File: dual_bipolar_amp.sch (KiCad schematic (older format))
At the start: 9 parts, among them U4 OPA2156xD

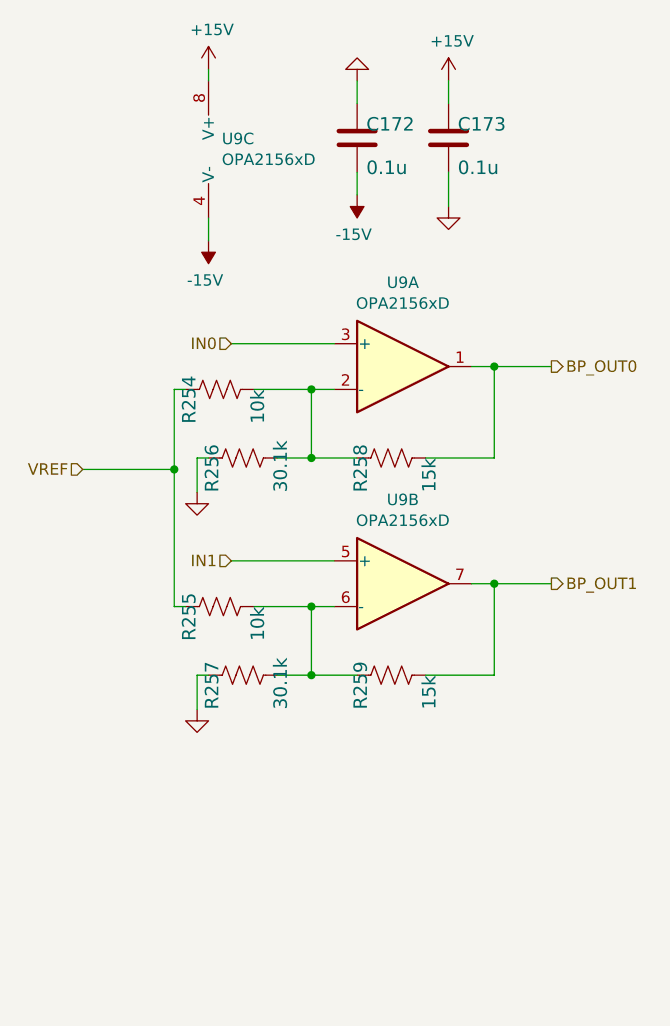
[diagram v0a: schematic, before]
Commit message: finished parts placement; reconnecting pins for less spagheti
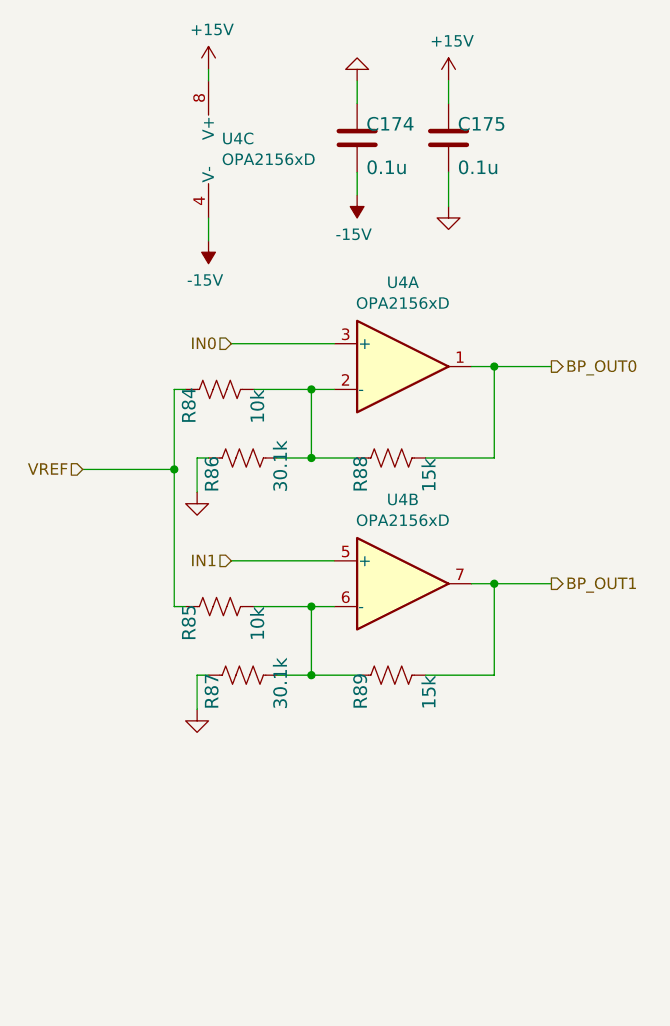
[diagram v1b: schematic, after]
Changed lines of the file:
@@
 $Descr A4 11693 8268
 encoding utf-8
-Sheet 24 26
+Sheet 23 26
 Title ""
 Date ""
@@
 AR Path="/6095BD4C/60EB6FD5/60F31C8B" Ref="U2"  Part="1"
 AR Path="/61B02572/60EB6FD5/60F31C8B" Ref="U9"  Part="1"
-F 0 "U9" H 5600 3617 50  0000 C CNN
+F 0 "U4" H 5600 3617 50  0000 C CNN
 F 1 "OPA2156xD" H 5600 3526 50  0000 C CNN
 F 2 "Package_SO:SOIC-8_3.9x4.9mm_P1.27mm" H 5700 3250 50  0001 C CNN
@@
 AR Path="/6095BD4C/60EB6FD5/60F31C94" Ref="R3"  Part="1"
 AR Path="/61B02572/60EB6FD5/60F31C94" Ref="R254"  Part="1"
-F 0 "R254" H 4650 3450 59  0000 L BNN
+F 0 "R84" H 4650 3450 59  0000 L BNN
 F 1 "10k" H 4650 3150 59  0000 L BNN
 F 2 "Resistor_SMD:R_0603_1608Metric" H 4800 3350 50  0001 C CNN
@@
 AR Path="/6095BD4C/60EB6FD5/60F31C9B" Ref="U2"  Part="3"
 AR Path="/61B02572/60EB6FD5/60F31C9B" Ref="U9"  Part="3"
-F 0 "U9" H 4808 2346 50  0000 L CNN
+F 0 "U4" H 4808 2346 50  0000 L CNN
 F 1 "OPA2156xD" H 4808 2255 50  0000 L CNN
 F 2 "Package_SO:SOIC-8_3.9x4.9mm_P1.27mm" H 4850 2300 50  0001 C CNN
@@
 AR Path="/6095BD4C/60EB6FD5/60F31CA4" Ref="R7"  Part="1"
 AR Path="/61B02572/60EB6FD5/60F31CA4" Ref="R256"  Part="1"
-F 0 "R256" H 4750 3750 59  0000 L BNN
+F 0 "R86" H 4750 3750 59  0000 L BNN
 F 1 "30.1k" H 4750 3450 59  0000 L BNN
 F 2 "Resistor_SMD:R_0603_1608Metric" H 4900 3650 50  0001 C CNN
@@
 AR Path="/6095BD4C/60EB6FD5/60F31CAA" Ref="#GND0250"  Part="1"
 AR Path="/61B02572/60EB6FD5/60F31CAA" Ref="#GND0276"  Part="1"
-F 0 "#GND0276" H 4700 3800 50  0001 C CNN
+F 0 "#GND063" H 4700 3800 50  0001 C CNN
 F 1 "GND" H 4600 3700 59  0001 L BNN
 F 2 "" H 4700 3800 50  0001 C CNN
@@
 AR Path="/6095BD4C/60EB6FD5/60F31CB1" Ref="R13"  Part="1"
 AR Path="/61B02572/60EB6FD5/60F31CB1" Ref="R258"  Part="1"
-F 0 "R258" H 5400 3750 59  0000 L BNN
+F 0 "R88" H 5400 3750 59  0000 L BNN
 F 1 "15k" H 5400 3450 59  0000 L BNN
 F 2 "Resistor_SMD:R_0603_1608Metric" H 5550 3650 50  0001 C CNN
@@
 AR Path="/6095BD4C/60EB6FD5/60F31CB8" Ref="U2"  Part="2"
 AR Path="/61B02572/60EB6FD5/60F31CB8" Ref="U9"  Part="2"
-F 0 "U9" H 5600 4567 50  0000 C CNN
+F 0 "U4" H 5600 4567 50  0000 C CNN
 F 1 "OPA2156xD" H 5600 4476 50  0000 C CNN
 F 2 "Package_SO:SOIC-8_3.9x4.9mm_P1.27mm" H 5700 4200 50  0001 C CNN
@@
 AR Path="/6095BD4C/60EB6FD5/60F31CC1" Ref="R4"  Part="1"
 AR Path="/61B02572/60EB6FD5/60F31CC1" Ref="R255"  Part="1"
-F 0 "R255" H 4650 4400 59  0000 L BNN
+F 0 "R85" H 4650 4400 59  0000 L BNN
 F 1 "10k" H 4650 4100 59  0000 L BNN
 F 2 "Resistor_SMD:R_0603_1608Metric" H 4800 4300 50  0001 C CNN
@@
 AR Path="/6095BD4C/60EB6FD5/60F31CCA" Ref="R8"  Part="1"
 AR Path="/61B02572/60EB6FD5/60F31CCA" Ref="R257"  Part="1"
-F 0 "R257" H 4750 4700 59  0000 L BNN
+F 0 "R87" H 4750 4700 59  0000 L BNN
 F 1 "30.1k" H 4750 4400 59  0000 L BNN
 F 2 "Resistor_SMD:R_0603_1608Metric" H 4900 4600 50  0001 C CNN
@@
 AR Path="/6095BD4C/60EB6FD5/60F31CD0" Ref="#GND0251"  Part="1"
 AR Path="/61B02572/60EB6FD5/60F31CD0" Ref="#GND0277"  Part="1"
-F 0 "#GND0277" H 4700 4750 50  0001 C CNN
+F 0 "#GND098" H 4700 4750 50  0001 C CNN
 F 1 "GND" H 4600 4650 59  0001 L BNN
 F 2 "" H 4700 4750 50  0001 C CNN
@@
 AR Path="/6095BD4C/60EB6FD5/60F31CD7" Ref="R14"  Part="1"
 AR Path="/61B02572/60EB6FD5/60F31CD7" Ref="R259"  Part="1"
-F 0 "R259" H 5400 4700 59  0000 L BNN
+F 0 "R89" H 5400 4700 59  0000 L BNN
 F 1 "15k" H 5400 4400 59  0000 L BNN
 F 2 "Resistor_SMD:R_0603_1608Metric" H 5550 4600 50  0001 C CNN
@@
 AR Path="/6095BD4C/60EB6FD5/60F31CDD" Ref="#PWR0235"  Part="1"
 AR Path="/61B02572/60EB6FD5/60F31CDD" Ref="#PWR0270"  Part="1"
-F 0 "#PWR0270" H 4750 1800 50  0001 C CNN
+F 0 "#PWR0240" H 4750 1800 50  0001 C CNN
 F 1 "+15V" H 4765 2123 50  0000 C CNN
 F 2 "" H 4750 1950 50  0001 C CNN
@@
 AR Path="/6095BD4C/60EB6FD5/60F31CE3" Ref="#PWR0236"  Part="1"
 AR Path="/61B02572/60EB6FD5/60F31CE3" Ref="#PWR0271"  Part="1"
-F 0 "#PWR0271" H 4750 2800 50  0001 C CNN
+F 0 "#PWR0241" H 4750 2800 50  0001 C CNN
 F 1 "-15V" H 4765 2873 50  0000 C CNN
 F 2 "" H 4750 2700 50  0001 C CNN
@@
 AR Path="/6095BD4C/60EB6FD5/60F31CED" Ref="C5"  Part="1"
 AR Path="/61B02572/60EB6FD5/60F31CED" Ref="C172"  Part="1"
-F 0 "C172" H 5440 2275 59  0000 L BNN
+F 0 "C174" H 5440 2275 59  0000 L BNN
 F 1 "0.1u" H 5440 2085 59  0000 L BNN
 F 2 "Capacitor_SMD:C_0603_1608Metric" H 5400 2250 50  0001 C CNN
@@
 AR Path="/6095BD4C/60EB6FD5/60F31CF7" Ref="C6"  Part="1"
 AR Path="/61B02572/60EB6FD5/60F31CF7" Ref="C173"  Part="1"
-F 0 "C173" H 5840 2275 59  0000 L BNN
+F 0 "C175" H 5840 2275 59  0000 L BNN
 F 1 "0.1u" H 5840 2085 59  0000 L BNN
 F 2 "Capacitor_SMD:C_0603_1608Metric" H 5800 2250 50  0001 C CNN
@@
 AR Path="/6095BD4C/60EB6FD5/60F31CFD" Ref="#PWR0238"  Part="1"
 AR Path="/61B02572/60EB6FD5/60F31CFD" Ref="#PWR0272"  Part="1"
-F 0 "#PWR0272" H 5400 2600 50  0001 C CNN
+F 0 "#PWR0244" H 5400 2600 50  0001 C CNN
 F 1 "-15V" H 5415 2673 50  0000 C CNN
 F 2 "" H 5400 2500 50  0001 C CNN
@@
 AR Path="/6095BD4C/60EB6FD5/60F31D03" Ref="#GND0252"  Part="1"
 AR Path="/61B02572/60EB6FD5/60F31D03" Ref="#GND0278"  Part="1"
-F 0 "#GND0278" H 5400 2000 50  0001 C CNN
+F 0 "#GND099" H 5400 2000 50  0001 C CNN
 F 1 "GND" H 5300 1900 59  0001 L BNN
 F 2 "" H 5400 2000 50  0001 C CNN
@@
 AR Path="/6095BD4C/60EB6FD5/60F31D09" Ref="#PWR0239"  Part="1"
 AR Path="/61B02572/60EB6FD5/60F31D09" Ref="#PWR0273"  Part="1"
-F 0 "#PWR0273" H 5800 1850 50  0001 C CNN
+F 0 "#PWR0245" H 5800 1850 50  0001 C CNN
 F 1 "+15V" H 5815 2173 50  0000 C CNN
 F 2 "" H 5800 2000 50  0001 C CNN
@@
 AR Path="/6095BD4C/60EB6FD5/60F31D0F" Ref="#GND0253"  Part="1"
 AR Path="/61B02572/60EB6FD5/60F31D0F" Ref="#GND0279"  Part="1"
-F 0 "#GND0279" H 5800 2550 50  0001 C CNN
+F 0 "#GND0100" H 5800 2550 50  0001 C CNN
 F 1 "GND" H 5700 2450 59  0001 L BNN
 F 2 "" H 5800 2550 50  0001 C CNN

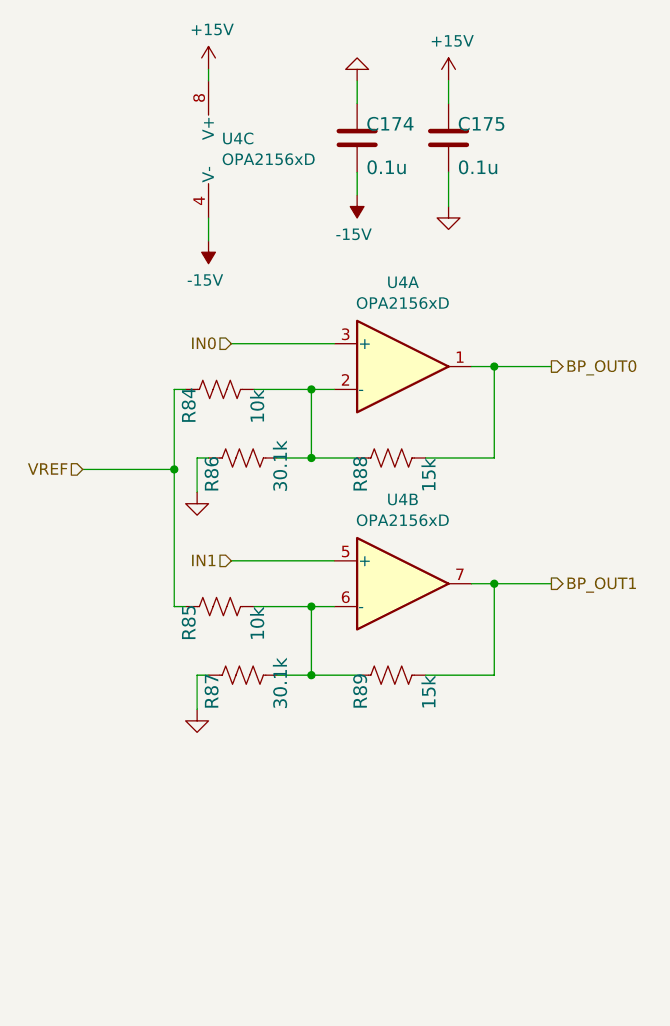
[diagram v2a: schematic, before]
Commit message: resynced layout and schematic after missing cap in bipolar amp
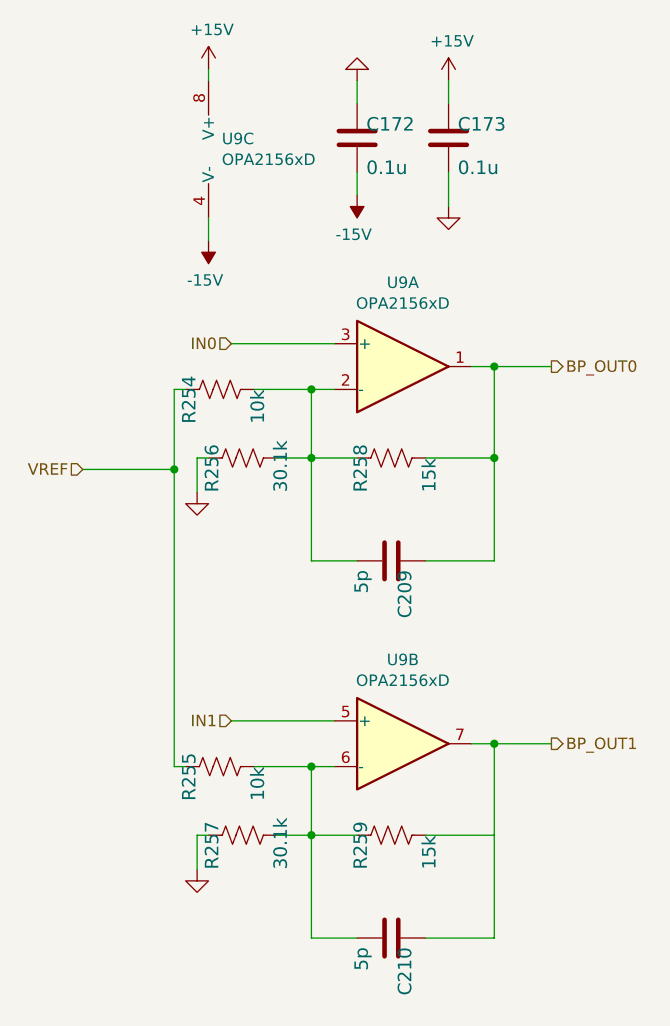
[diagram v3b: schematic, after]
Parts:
- added C203, C204: 5p, Capacitor_SMD:C_0603_1608Metric, symbol Device:C
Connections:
- net BP_OUT0: now also C203.1
- net BP_OUT1: now also C204.1
- net at R84.2, R86.2, R88.1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: now also C203.2
- net at R85.2, R87.2, R89.1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: now also C204.2
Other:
- moved on the sheet: R255, R257, R259, U9B

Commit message: move bom files to bom folder
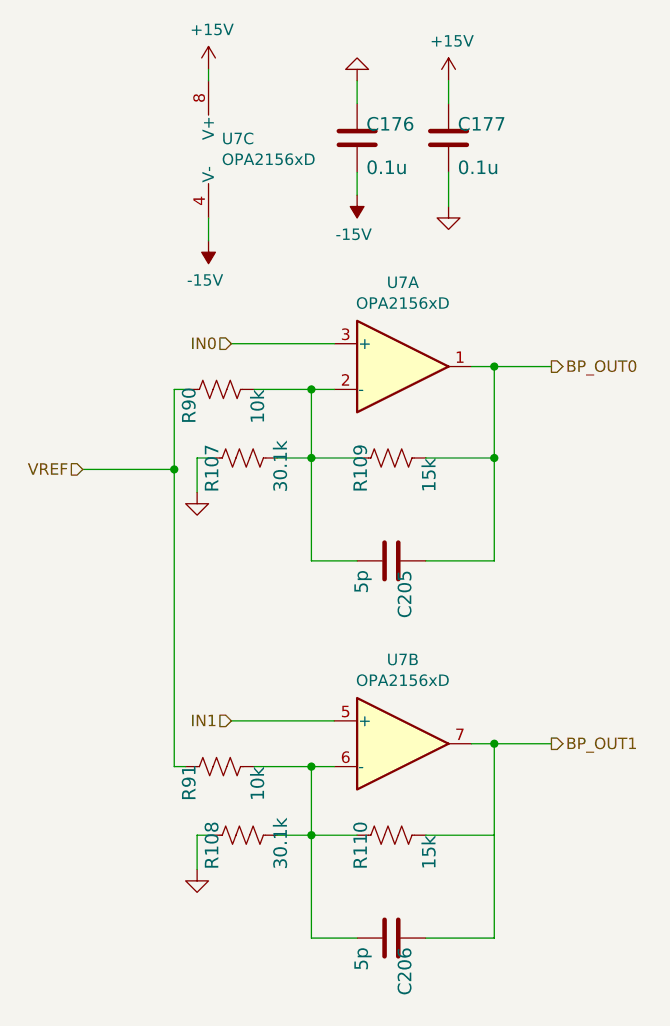
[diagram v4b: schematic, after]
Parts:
- C174, C175: Manf# CC0603MRX7R8BB104 -> CL10B104KA8NFNC; Manufacturer_Name Yageo -> Samsung; Tolerance 20% -> 10%
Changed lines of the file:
@@
 $Descr A4 11693 8268
 encoding utf-8
-Sheet 26 26
+Sheet 23 26
 Title ""
 Date ""
@@
 AR Path="/6095BD4C/60EB6FD5/60F31C8B" Ref="U2"  Part="1"
 AR Path="/61B02572/60EB6FD5/60F31C8B" Ref="U9"  Part="1"
-F 0 "U9" H 5600 3617 50  0000 C CNN
+F 0 "U7" H 5600 3617 50  0000 C CNN
 F 1 "OPA2156xD" H 5600 3526 50  0000 C CNN
 F 2 "Package_SO:SOIC-8_3.9x4.9mm_P1.27mm" H 5700 3250 50  0001 C CNN
@@
 AR Path="/6095BD4C/60EB6FD5/60F31C94" Ref="R3"  Part="1"
 AR Path="/61B02572/60EB6FD5/60F31C94" Ref="R254"  Part="1"
-F 0 "R254" H 4650 3450 59  0000 L BNN
+F 0 "R90" H 4650 3450 59  0000 L BNN
 F 1 "10k" H 4650 3150 59  0000 L BNN
 F 2 "Resistor_SMD:R_0603_1608Metric" H 4800 3350 50  0001 C CNN
@@
 AR Path="/6095BD4C/60EB6FD5/60F31C9B" Ref="U2"  Part="3"
 AR Path="/61B02572/60EB6FD5/60F31C9B" Ref="U9"  Part="3"
-F 0 "U9" H 4808 2346 50  0000 L CNN
+F 0 "U7" H 4808 2346 50  0000 L CNN
 F 1 "OPA2156xD" H 4808 2255 50  0000 L CNN
 F 2 "Package_SO:SOIC-8_3.9x4.9mm_P1.27mm" H 4850 2300 50  0001 C CNN
@@
 AR Path="/6095BD4C/60EB6FD5/60F31CA4" Ref="R7"  Part="1"
 AR Path="/61B02572/60EB6FD5/60F31CA4" Ref="R256"  Part="1"
-F 0 "R256" H 4750 3750 59  0000 L BNN
+F 0 "R107" H 4750 3750 59  0000 L BNN
 F 1 "30.1k" H 4750 3450 59  0000 L BNN
 F 2 "Resistor_SMD:R_0603_1608Metric" H 4900 3650 50  0001 C CNN
@@
 AR Path="/6095BD4C/60EB6FD5/60F31CB1" Ref="R13"  Part="1"
 AR Path="/61B02572/60EB6FD5/60F31CB1" Ref="R258"  Part="1"
-F 0 "R258" H 5400 3750 59  0000 L BNN
+F 0 "R109" H 5400 3750 59  0000 L BNN
 F 1 "15k" H 5400 3450 59  0000 L BNN
 F 2 "Resistor_SMD:R_0603_1608Metric" H 5550 3650 50  0001 C CNN
@@
 AR Path="/6095BD4C/60EB6FD5/60F31CB8" Ref="U2"  Part="2"
 AR Path="/61B02572/60EB6FD5/60F31CB8" Ref="U9"  Part="2"
-F 0 "U9" H 5600 5267 50  0000 C CNN
+F 0 "U7" H 5600 5267 50  0000 C CNN
 F 1 "OPA2156xD" H 5600 5176 50  0000 C CNN
 F 2 "Package_SO:SOIC-8_3.9x4.9mm_P1.27mm" H 5700 4900 50  0001 C CNN
@@
 AR Path="/6095BD4C/60EB6FD5/60F31CC1" Ref="R4"  Part="1"
 AR Path="/61B02572/60EB6FD5/60F31CC1" Ref="R255"  Part="1"
-F 0 "R255" H 4650 5100 59  0000 L BNN
+F 0 "R91" H 4650 5100 59  0000 L BNN
 F 1 "10k" H 4650 4800 59  0000 L BNN
 F 2 "Resistor_SMD:R_0603_1608Metric" H 4800 5000 50  0001 C CNN
@@
 AR Path="/6095BD4C/60EB6FD5/60F31CCA" Ref="R8"  Part="1"
 AR Path="/61B02572/60EB6FD5/60F31CCA" Ref="R257"  Part="1"
-F 0 "R257" H 4750 5400 59  0000 L BNN
+F 0 "R108" H 4750 5400 59  0000 L BNN
 F 1 "30.1k" H 4750 5100 59  0000 L BNN
 F 2 "Resistor_SMD:R_0603_1608Metric" H 4900 5300 50  0001 C CNN
@@
 AR Path="/6095BD4C/60EB6FD5/60F31CD7" Ref="R14"  Part="1"
 AR Path="/61B02572/60EB6FD5/60F31CD7" Ref="R259"  Part="1"
-F 0 "R259" H 5400 5400 59  0000 L BNN
+F 0 "R110" H 5400 5400 59  0000 L BNN
 F 1 "15k" H 5400 5100 59  0000 L BNN
 F 2 "Resistor_SMD:R_0603_1608Metric" H 5550 5300 50  0001 C CNN
@@
 AR Path="/6095BD4C/60EB6FD5/60F31CED" Ref="C5"  Part="1"
 AR Path="/61B02572/60EB6FD5/60F31CED" Ref="C172"  Part="1"
-F 0 "C172" H 5440 2275 59  0000 L BNN
+F 0 "C176" H 5440 2275 59  0000 L BNN
 F 1 "0.1u" H 5440 2085 59  0000 L BNN
 F 2 "Capacitor_SMD:C_0603_1608Metric" H 5400 2250 50  0001 C CNN
 F 3 "" H 5400 2250 50  0001 C CNN
-F 4 "CC0603MRX7R8BB104" H 5400 2250 50  0001 C CNN "Manf#"
-F 5 "Yageo" H 5440 2375 50  0001 C CNN "Manufacturer_Name"
-F 6 "20%" H 5440 2375 50  0001 C CNN "Tolerance"
+F 4 "CL10B104KA8NFNC" H 5400 2250 50  0001 C CNN "Manf#"
+F 5 "Samsung" H 5440 2375 50  0001 C CNN "Manufacturer_Name"
+F 6 "10%" H 5440 2375 50  0001 C CNN "Tolerance"
 F 7 "25" H 5440 2375 50  0001 C CNN "voltage"
 	1    5400 2250
@@
 AR Path="/6095BD4C/60EB6FD5/60F31CF7" Ref="C6"  Part="1"
 AR Path="/61B02572/60EB6FD5/60F31CF7" Ref="C173"  Part="1"
-F 0 "C173" H 5840 2275 59  0000 L BNN
+F 0 "C177" H 5840 2275 59  0000 L BNN
 F 1 "0.1u" H 5840 2085 59  0000 L BNN
 F 2 "Capacitor_SMD:C_0603_1608Metric" H 5800 2250 50  0001 C CNN
 F 3 "" H 5800 2250 50  0001 C CNN
-F 4 "CC0603MRX7R8BB104" H 5800 2250 50  0001 C CNN "Manf#"
-F 5 "Yageo" H 5840 2375 50  0001 C CNN "Manufacturer_Name"
-F 6 "20%" H 5840 2375 50  0001 C CNN "Tolerance"
+F 4 "CL10B104KA8NFNC" H 5800 2250 50  0001 C CNN "Manf#"
+F 5 "Samsung" H 5840 2375 50  0001 C CNN "Manufacturer_Name"
+F 6 "10%" H 5840 2375 50  0001 C CNN "Tolerance"
 F 7 "25" H 5840 2375 50  0001 C CNN "voltage"
 	1    5800 2250
@@
 AR Path="/6095BD4C/60EB6FD5/60E3E42E" Ref="C201"  Part="1"
 AR Path="/61B02572/60EB6FD5/60E3E42E" Ref="C209"  Part="1"
-F 0 "C209" H 5590 4125 59  0000 L BNN
+F 0 "C205" H 5590 4125 59  0000 L BNN
 F 1 "5p" H 5590 3935 59  0000 L BNN
 F 2 "Capacitor_SMD:C_0603_1608Metric" H 5550 4100 50  0001 C CNN
@@
 AR Path="/6095BD4C/60EB6FD5/60E41417" Ref="C202"  Part="1"
 AR Path="/61B02572/60EB6FD5/60E41417" Ref="C210"  Part="1"
-F 0 "C210" H 5590 5775 59  0000 L BNN
+F 0 "C206" H 5590 5775 59  0000 L BNN
 F 1 "5p" H 5590 5585 59  0000 L BNN
 F 2 "Capacitor_SMD:C_0603_1608Metric" H 5550 5750 50  0001 C CNN
